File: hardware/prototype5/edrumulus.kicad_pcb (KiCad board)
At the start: 2 copper layers, 65 x 56.5 mm, 95 parts, among them J1 Trigger Connector, J2 Raspberry Pi GPIO pins, U1 ESP32-WROOM-32U, U2 AMS1117-3.3, U3 LT1761-3.3

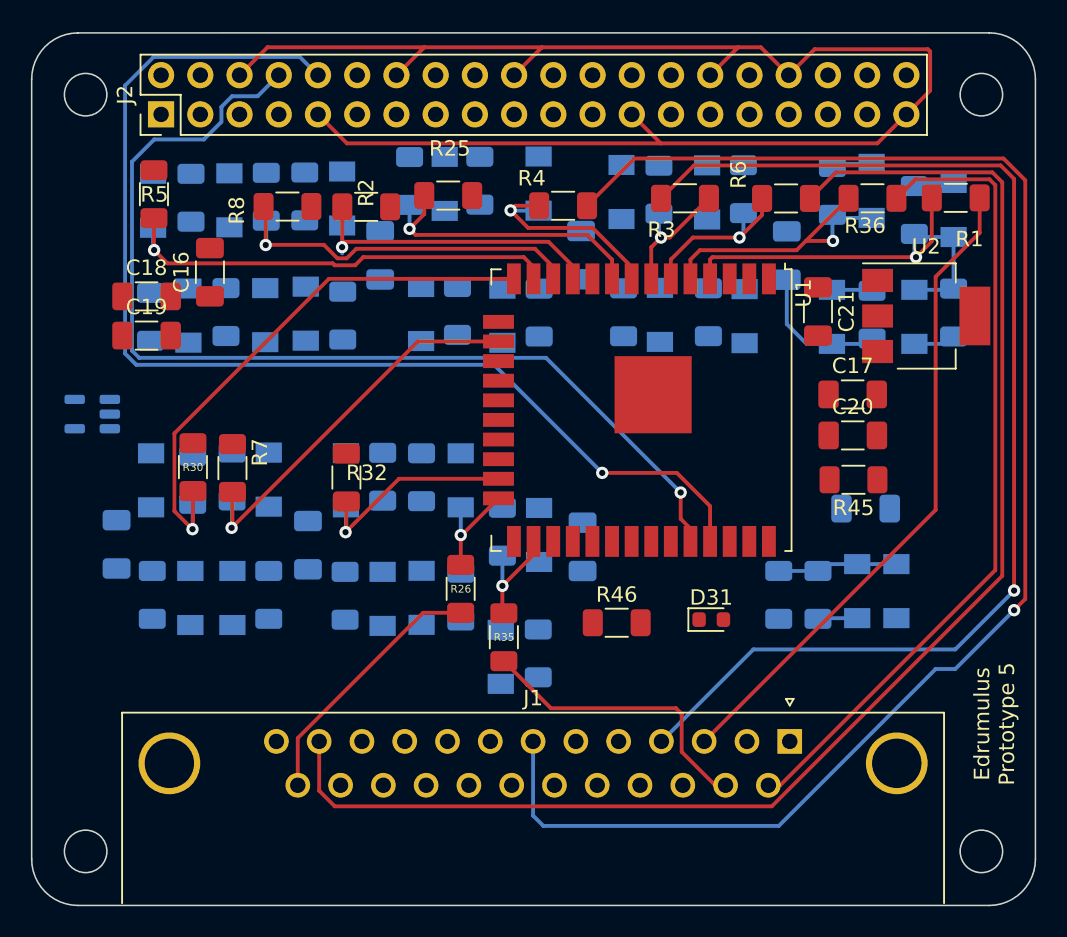
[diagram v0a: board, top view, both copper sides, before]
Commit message: connect GPIOs for boot/enable, some more routing for prototype 5
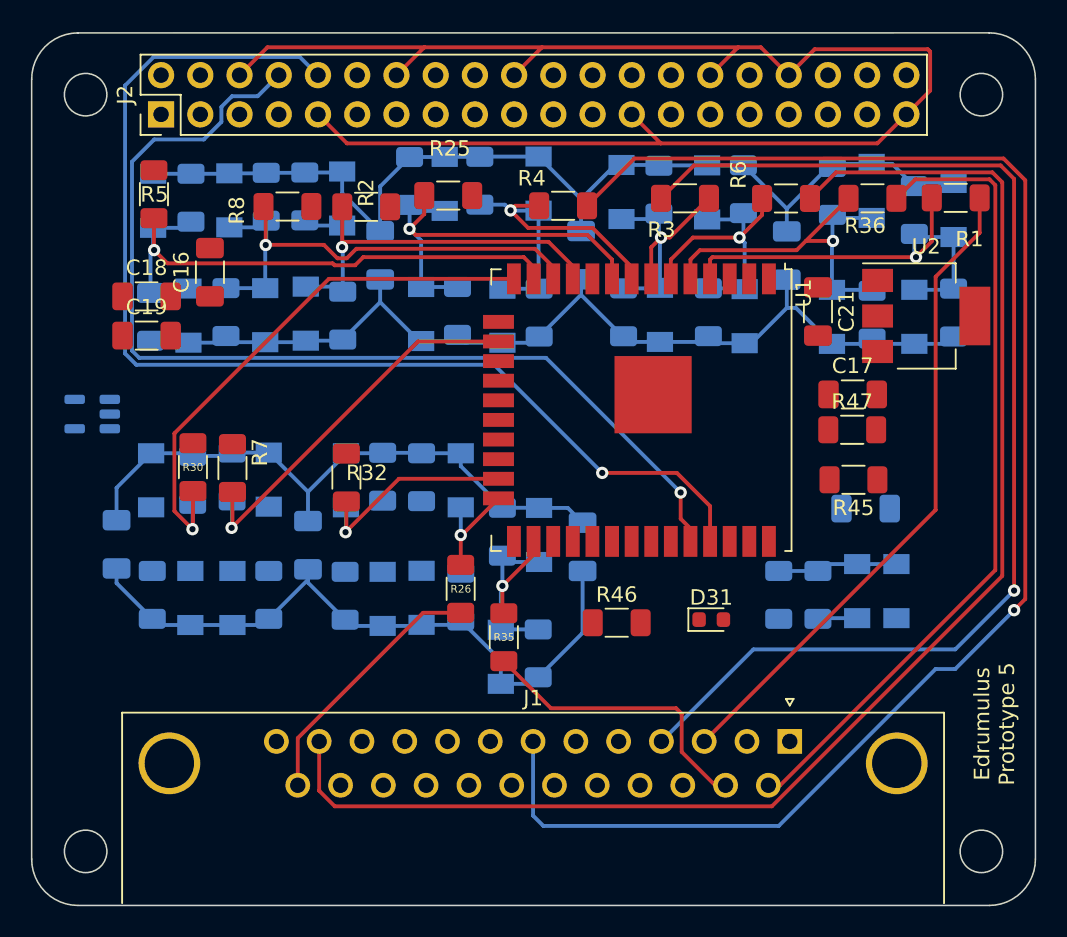
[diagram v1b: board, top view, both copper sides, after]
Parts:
- removed C20: 1 µF, Capacitor_SMD:C_1206_3216Metric_Pad1.33x1.80mm_HandSolder
- added R47: 10 kOhm, Resistor_SMD:R_1206_3216Metric_Pad1.30x1.75mm_HandSolder, F.Cu at (159.7, 98.8)
- turned C15 to 90 degrees
- turned C2 to 90 degrees
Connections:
- C15 pad 1: 3V3 -> CRASH1-SLEEVE
- C15 pad 2: CRASH1-SLEEVE -> 3V3
- C2 pad 1: 3V3 -> CRASH1-SLEEVE
- C2 pad 2: CRASH1-SLEEVE -> 3V3
- J2 pad 21: unconnected-(J2-Pad21) -> PI-GPIO9
- J2 pad 7: unconnected-(J2-Pad7) -> PI-GPIO4
- R45 pad 1: ESP32-3V3 -> CRASH1-SLEEVE
- R45 pad 2: Net-(C20-Pad1) -> PI-GPIO9
- U1 pad 25: unconnected-(U1-Pad25) -> PI-GPIO4
- U1 pad 3: Net-(C20-Pad1) -> PI-GPIO9
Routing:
- net 3V3: track 7.80 -> 112.8 mm
- net CRASH1-SLEEVE: track 113.4 -> 205.9 mm
- net GPIO32: track 13.9 -> 23.5 mm
- net GPIO33: track 19.3 -> 28.2 mm
- net GPIO34: track 11.1 -> 19.5 mm
- net GPIO35: track 8.70 -> 16.9 mm
- net GPIO14: track 29.8 -> 37.8 mm
- net GPIO27: track 24.6 -> 32.5 mm
- net GPIO4: track 7.48 -> 15.3 mm
- net GPIO26: track 20.7 -> 28.5 mm
- net GPIO39: track 21.8 -> 25.0 mm

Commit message: new linear controller for SDB bias
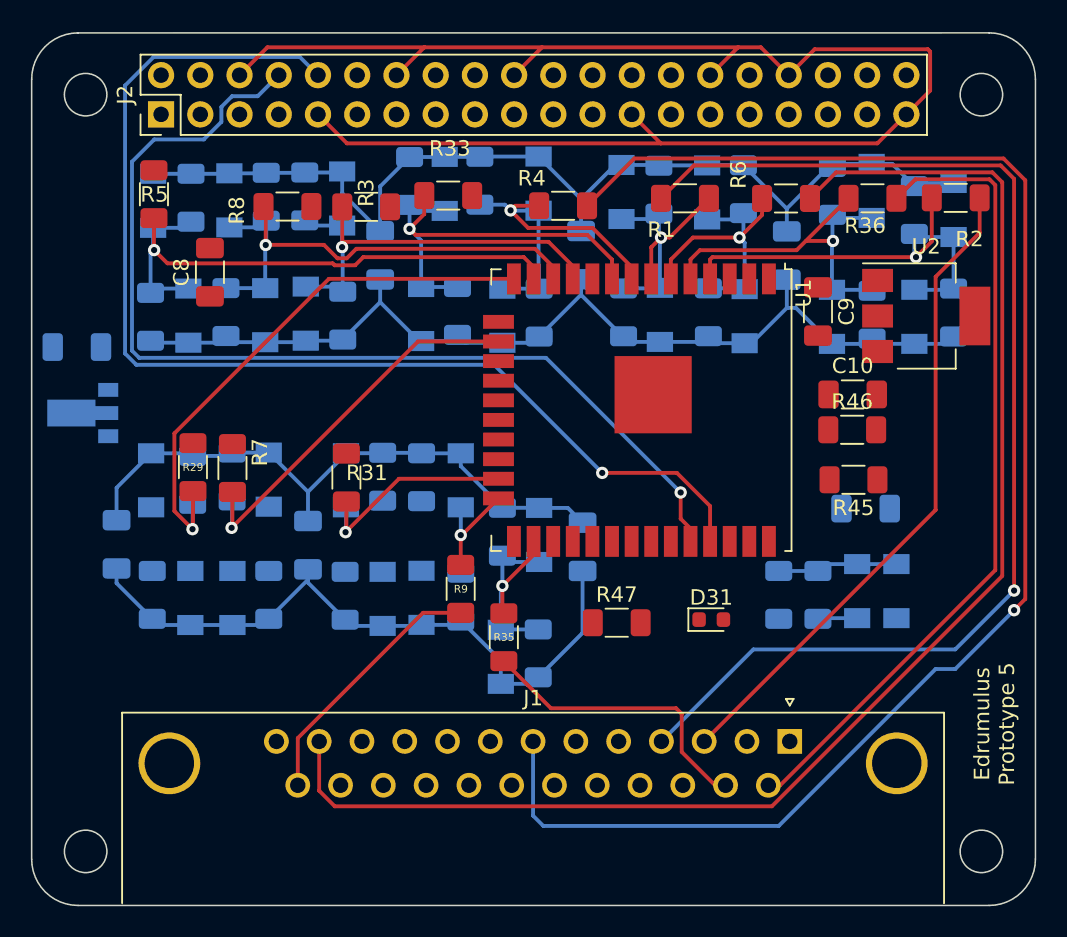
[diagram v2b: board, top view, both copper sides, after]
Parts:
- removed C18: 10 nF, Capacitor_SMD:C_1206_3216Metric_Pad1.33x1.80mm_HandSolder
- removed C19: 10 µF, Capacitor_SMD:C_1206_3216Metric_Pad1.33x1.80mm_HandSolder
- added C11: 1 µF, Capacitor_SMD:C_1206_3216Metric_Pad1.33x1.80mm_HandSolder, B.Cu at (109.5, 93.5)
- U3: value LT1761-3.3 -> MCP1754S-3302xMB; footprint Package_TO_SOT_SMD:TSOT-23-5 -> Package_TO_SOT_SMD:SOT-89-3
- moved U3 0.62 mm to (109.9, 97.7)
- renumbered C3 to C1, C17 to C10, C1 to C2, C4 to C3, C2 to C4, C10 to C5, C15 to C6, C14 to C7, C16 to C8, C21 to C9, D9 to D10, D10 to D11, D11 to D12, D12 to D13, D13 to D14, D14 to D15, D15 to D16, D16 to D17, D19 to D18, D25 to D19, D22 to D21, D17 to D22, D26 to D23, D23 to D24, D24 to D25, D21 to D26, D18 to D9, R3 to R1, R9 to R10, R10 to R11, R11 to R12, R12 to R13, R13 to R14, R14 to R15, R15 to R16, R16 to R17, R27 to R18, R17 to R19, R1 to R2, R18 to R20, R19 to R21, R20 to R22, R21 to R23, R22 to R24, R23 to R25, R24 to R26, R28 to R27, R37 to R28, R30 to R29, R2 to R3, R31 to R30, R32 to R31, R34 to R32, R25 to R33, R29 to R34, R38 to R37, R39 to R38, R40 to R39, R33 to R40, R47 to R46, R46 to R47, R26 to R9
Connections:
- U3 pad 3: RASPI-VIN -> 3V3

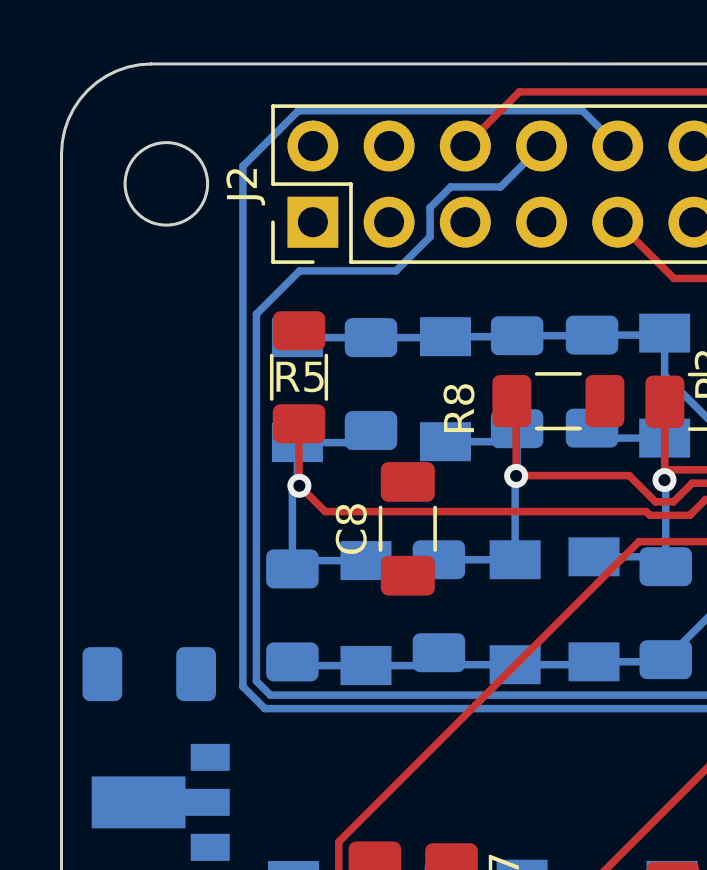
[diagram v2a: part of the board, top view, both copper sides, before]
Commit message: added keepout zones
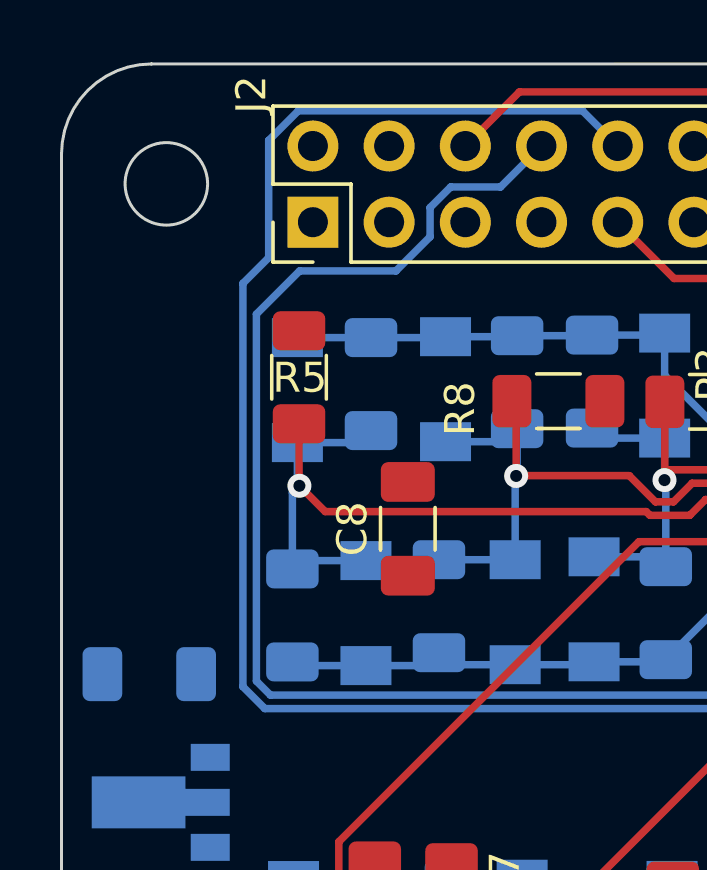
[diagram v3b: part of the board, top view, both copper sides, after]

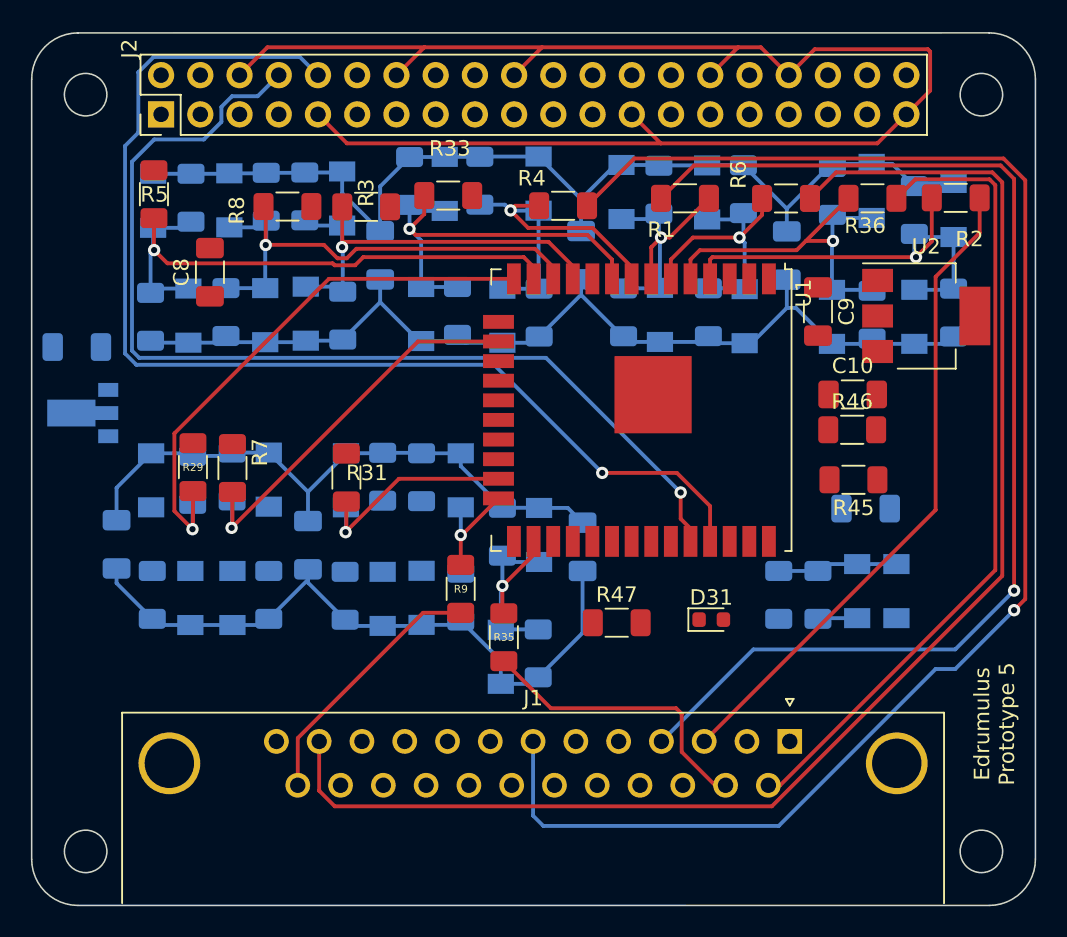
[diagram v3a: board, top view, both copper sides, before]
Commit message: some more routing for the prototype 5
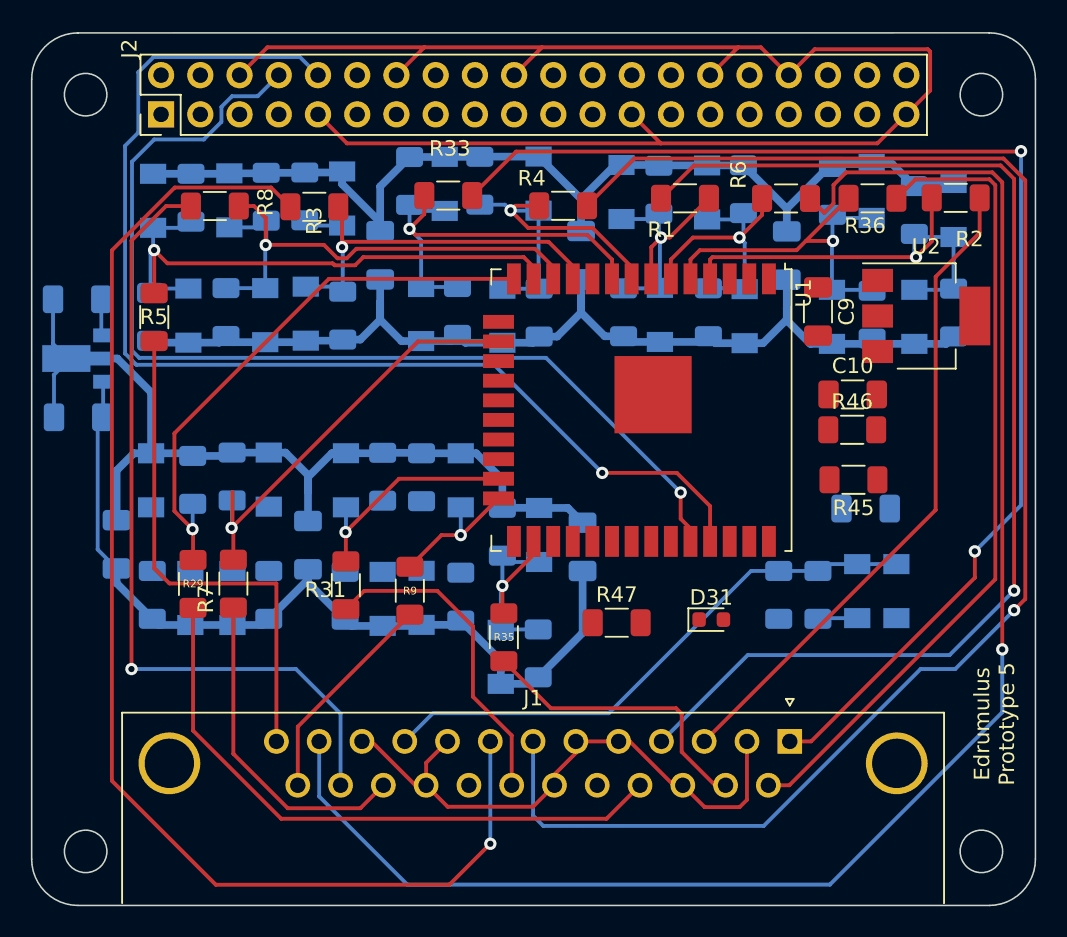
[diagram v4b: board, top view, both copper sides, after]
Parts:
- C8: moved to B.Cu
- moved C8 8.77 mm to (109.5, 90.4), turned to 180 degrees
- moved R5 7.96 mm to (114.5, 91.5), turned to 90 degrees
- moved R29 7.56 mm to (117.0, 108.8), turned to -90 degrees
- moved R7 7.49 mm to (119.6, 108.8), turned to 90 degrees
- moved R31 6.98 mm to (126.9, 108.9), turned to -90 degrees
- moved R8 4.70 mm to (118.4, 84.3), turned to 0 degrees
- moved C11 4.55 mm to (109.6, 98.0)
- moved U3 3.55 mm to (109.5, 94.2)
- moved R3 3.36 mm to (124.9, 84.4), turned to 0 degrees
- moved R9 3.29 mm to (131.1, 109.2)
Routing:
- net HI-HAT-RING: track 0.00 -> 83.1 mm, vias 0 -> 1
- net KICK-TIP: track 0.00 -> 82.0 mm, vias 0 -> 2
- net CRASH1-SLEEVE: track 205.9 -> 271.1 mm
- net RIDE-TIP: track 0.00 -> 51.9 mm, vias 0 -> 1
- net TOM2-TIP: track 0.00 -> 40.2 mm
- net CRASH1-RING: track 0.00 -> 33.3 mm
- net HI-HAT-CONTROL-TIP: track 7.80 -> 36.6 mm
- net RIDE-RING: track 0.00 -> 21.3 mm
- net TOM3-TIP: track 0.00 -> 21.0 mm
- net 3V3: track 112.8 -> 125.6 mm
- net CRASH1-TIP: track 92.9 -> 104.0 mm, vias 0 -> 1
- net RIDE-BELL-TIP: track 17.0 -> 14.1 mm
- net RASPI-VIN: track 0.00 -> 2.39 mm
- net GPIO2: track 7.16 -> 9.37 mm
- net GPIO13: track 26.3 -> 28.4 mm
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
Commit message: even more routing for the prototype 5
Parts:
- moved C5 7.97 mm to (161.7, 111.8)
- moved C10 6.74 mm to (157.1, 90.3), turned to 90 degrees
- moved C9 4.24 mm to (157.2, 95.4)
- moved R46 2.27 mm to (159.8, 101.1), turned to 180 degrees
- moved D31 2.05 mm to (148.5, 111.3), turned to 180 degrees
- moved R28 1.50 mm to (155.4, 108.1)
- moved R37 1.50 mm to (157.9, 108.1)
- moved D19 1.50 mm to (163.0, 107.8)
- moved D23 1.50 mm to (160.5, 107.8)
- moved R45 1.43 mm to (159.8, 103.5)
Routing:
- net RASPI-VIN: track 2.39 -> 112.6 mm, vias 0 -> 3
- net CRASH1-SLEEVE: track 271.1 -> 299.1 mm
- net PI-GPIO4: track 0.00 -> 23.7 mm
- net PI-GPIO9: track 0.00 -> 20.9 mm
- net ESP32-3V3: track 0.00 -> 10.3 mm
- net GPIO12: track 36.5 -> 44.5 mm
- net GPIO2: track 9.37 -> 17.1 mm
- net GPIO13: track 28.4 -> 36.2 mm
- net GPIO15: track 14.9 -> 22.4 mm
- net Net-(R47-Pad1): track 0.00 -> 5.28 mm
- net 3V3: track 125.6 -> 127.9 mm
- net Net-(D31-Pad2): track 0.00 -> 1.75 mm
- net HI-HAT-CONTROL-TIP: track 36.6 -> 38.2 mm

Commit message: routing prototype 5
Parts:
- moved D19 16.9 mm to (146.2, 109.8), turned to 90 degrees
- moved C5 15.4 mm to (147.5, 105.9), turned to 0 degrees
- moved D23 11.9 mm to (148.7, 109.8), turned to -90 degrees
- moved R37 6.84 mm to (151.3, 109.6), turned to -90 degrees
- moved R28 2.20 mm to (153.8, 109.6), turned to -90 degrees
- moved R1 0.62 mm to (148.8, 84.4)
- moved R2 0.62 mm to (166.3, 84.4)
- moved R36 0.62 mm to (160.9, 84.4)
- moved R6 0.62 mm to (155.3, 84.4)
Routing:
- net PI-GPIO4: track 23.7 -> 114.0 mm, vias 0 -> 2
- net PI-GPIO9: track 20.9 -> 77.9 mm, vias 0 -> 2
- net 3V3: track 127.9 -> 161.4 mm, vias 0 -> 2
- net CRASH1-SLEEVE: track 299.1 -> 326.0 mm, vias 0 -> 3
- net GPIO25: track 0.00 -> 25.5 mm, vias 0 -> 1
- net ESP32-3V3: track 10.3 -> 29.1 mm
- net HI-HAT-CONTROL-TIP: track 38.2 -> 26.3 mm
- net GPIO12: track 44.5 -> 39.2 mm
- net HI-HAT-RING: track 83.1 -> 80.2 mm
- net RASPI-VIN: track 112.6 -> 110.2 mm
- net GPIO13: track 36.2 -> 33.9 mm
- net CRASH1-TIP: track 104.0 -> 101.9 mm
- net ESP-UART0-RX: track 67.4 -> 68.6 mm
- net HI-HAT-TIP: track 100.4 -> 99.3 mm
- net KICK-TIP: track 82.0 -> 81.0 mm
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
